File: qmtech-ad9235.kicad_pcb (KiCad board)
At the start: 4 copper layers, 55 x 75 mm, 57 parts

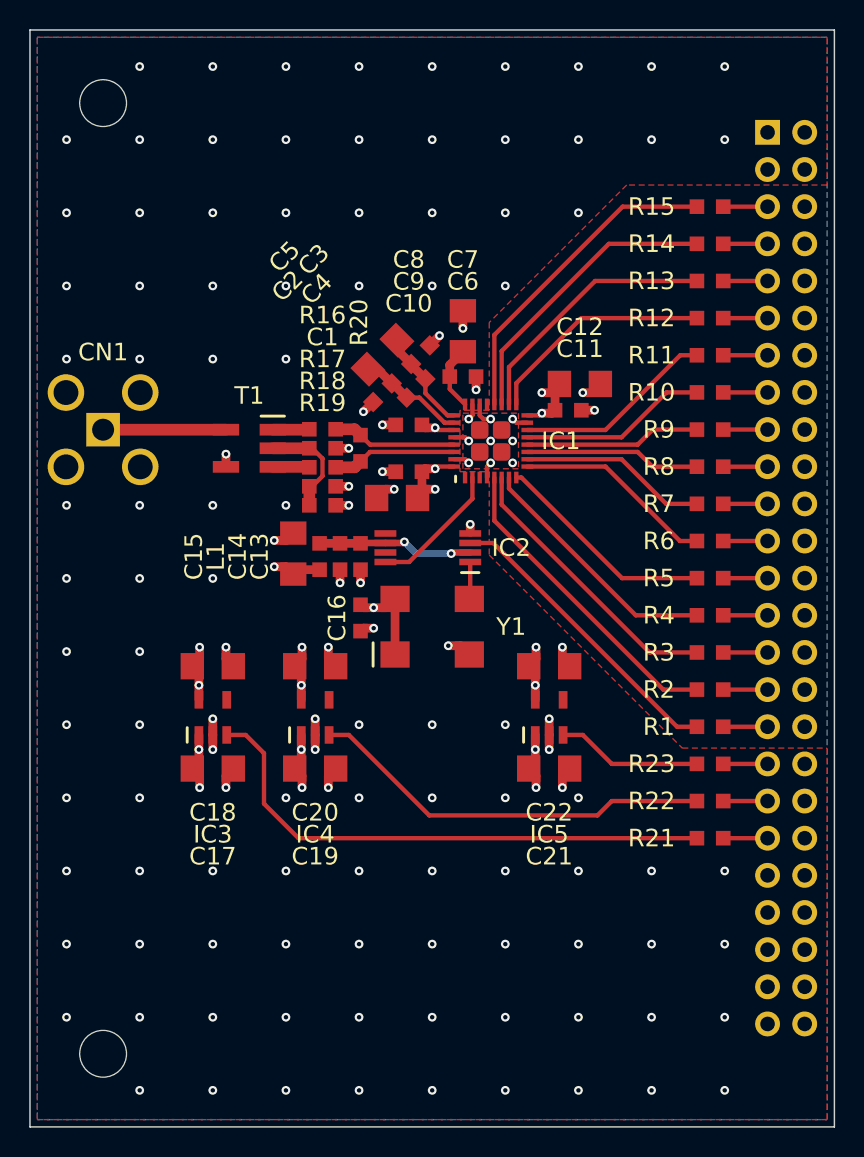
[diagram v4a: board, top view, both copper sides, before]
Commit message: update numbers in resistor reference designators in qmtech-ad9235
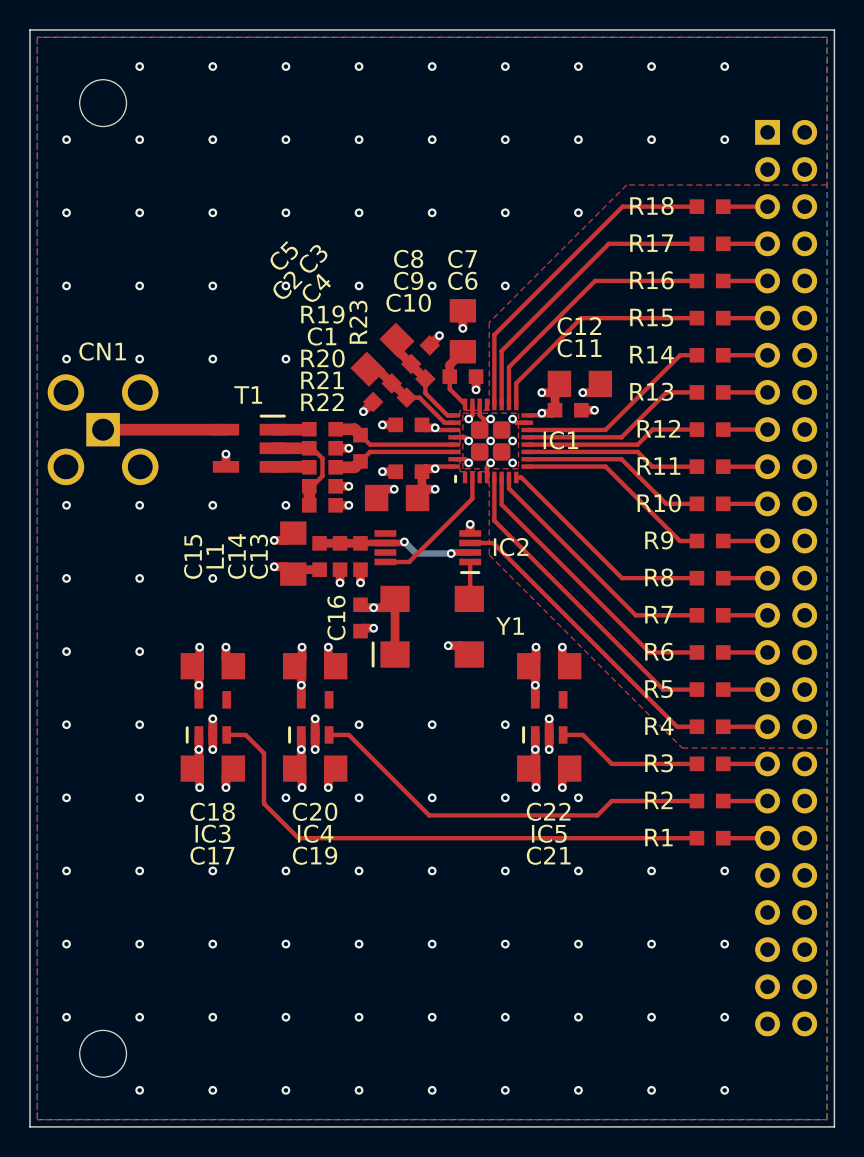
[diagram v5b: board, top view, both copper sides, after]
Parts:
- renumbered R21 to R1, R7 to R10, R8 to R11, R9 to R12, R10 to R13, R11 to R14, R12 to R15, R13 to R16, R14 to R17, R15 to R18, R16 to R19, R22 to R2, R17 to R20, R18 to R21, R19 to R22, R20 to R23, R23 to R3, R1 to R4, R2 to R5, R3 to R6, R4 to R7, R5 to R8, R6 to R9
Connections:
- CN2 pad 11: W12 -> W15
- CN2 pad 13: W11 -> W14
- CN2 pad 15: W10 -> W13
- CN2 pad 17: W9 -> W12
- CN2 pad 19: W8 -> W11
- CN2 pad 21: W7 -> W10
- CN2 pad 23: W6 -> W9
- CN2 pad 25: W5 -> W8
- CN2 pad 27: W4 -> W7
- CN2 pad 29: W3 -> W6
- CN2 pad 31: W2 -> W5
- CN2 pad 33: W1 -> W4
- CN2 pad 35: W18 -> W3
- CN2 pad 37: W17 -> W2
- CN2 pad 39: W16 -> W1
- CN2 pad 5: W15 -> W18
- CN2 pad 7: W14 -> W17
- CN2 pad 9: W13 -> W16
- R1 pad 2: W16 -> W1
- R10 pad 2: W7 -> W10
- R11 pad 2: W8 -> W11
- R12 pad 2: W9 -> W12
- R13 pad 2: W10 -> W13
- R14 pad 2: W11 -> W14
- R15 pad 2: W12 -> W15
- R16 pad 2: W13 -> W16
- R17 pad 2: W14 -> W17
- R18 pad 2: W15 -> W18
- R2 pad 2: W17 -> W2
- R3 pad 2: W18 -> W3
- R4 pad 2: W1 -> W4
- R5 pad 2: W2 -> W5
- R6 pad 2: W3 -> W6
- R7 pad 2: W4 -> W7
- R8 pad 2: W5 -> W8
- R9 pad 2: W6 -> W9
